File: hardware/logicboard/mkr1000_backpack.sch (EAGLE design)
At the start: 7 parts, among them J4 DNP, J5 DNP

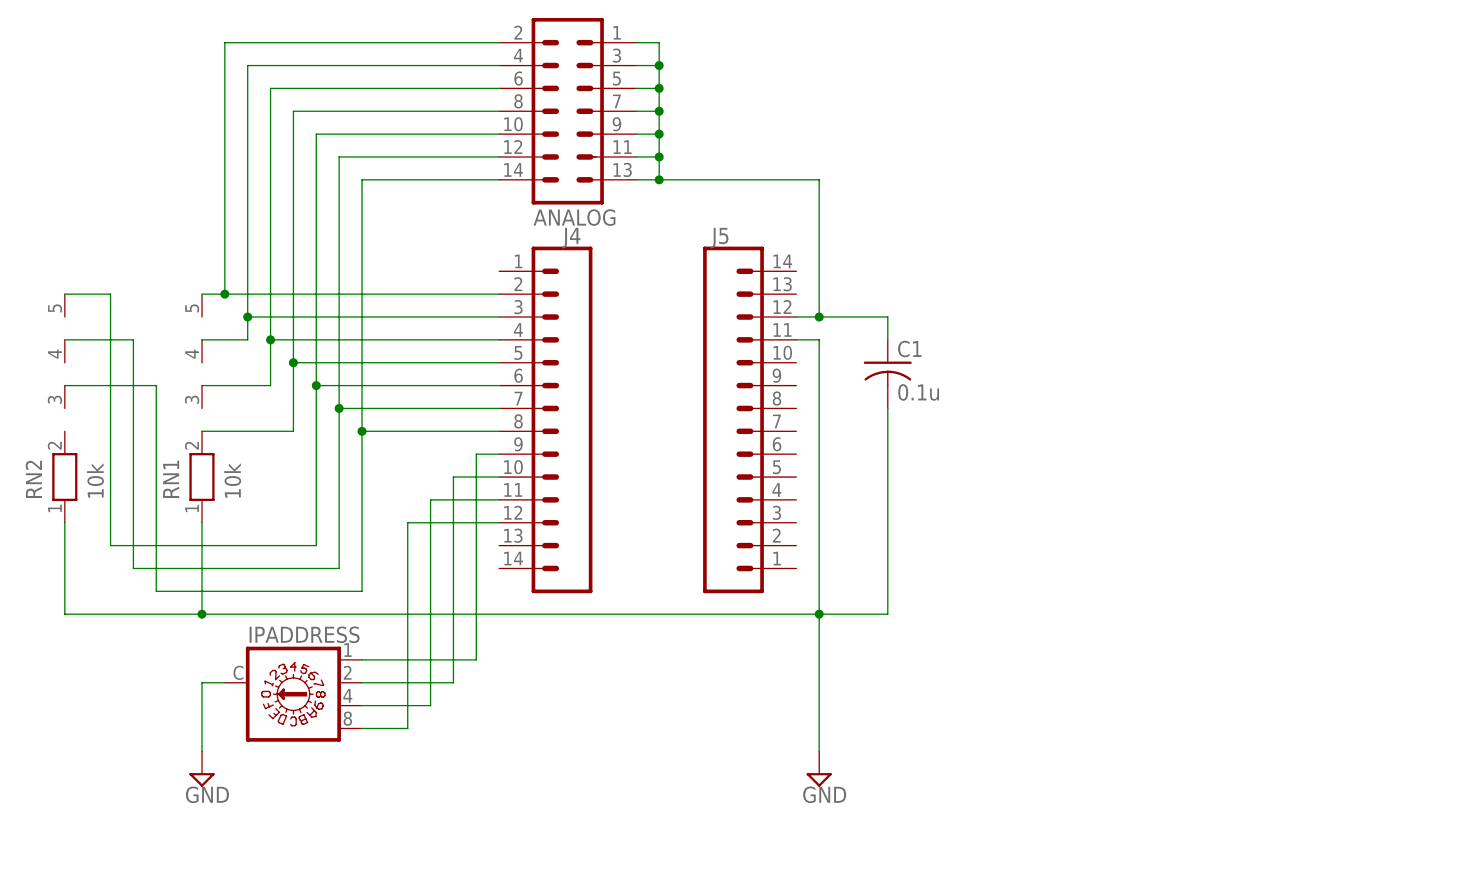
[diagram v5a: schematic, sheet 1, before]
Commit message: LED ports and I2C port.
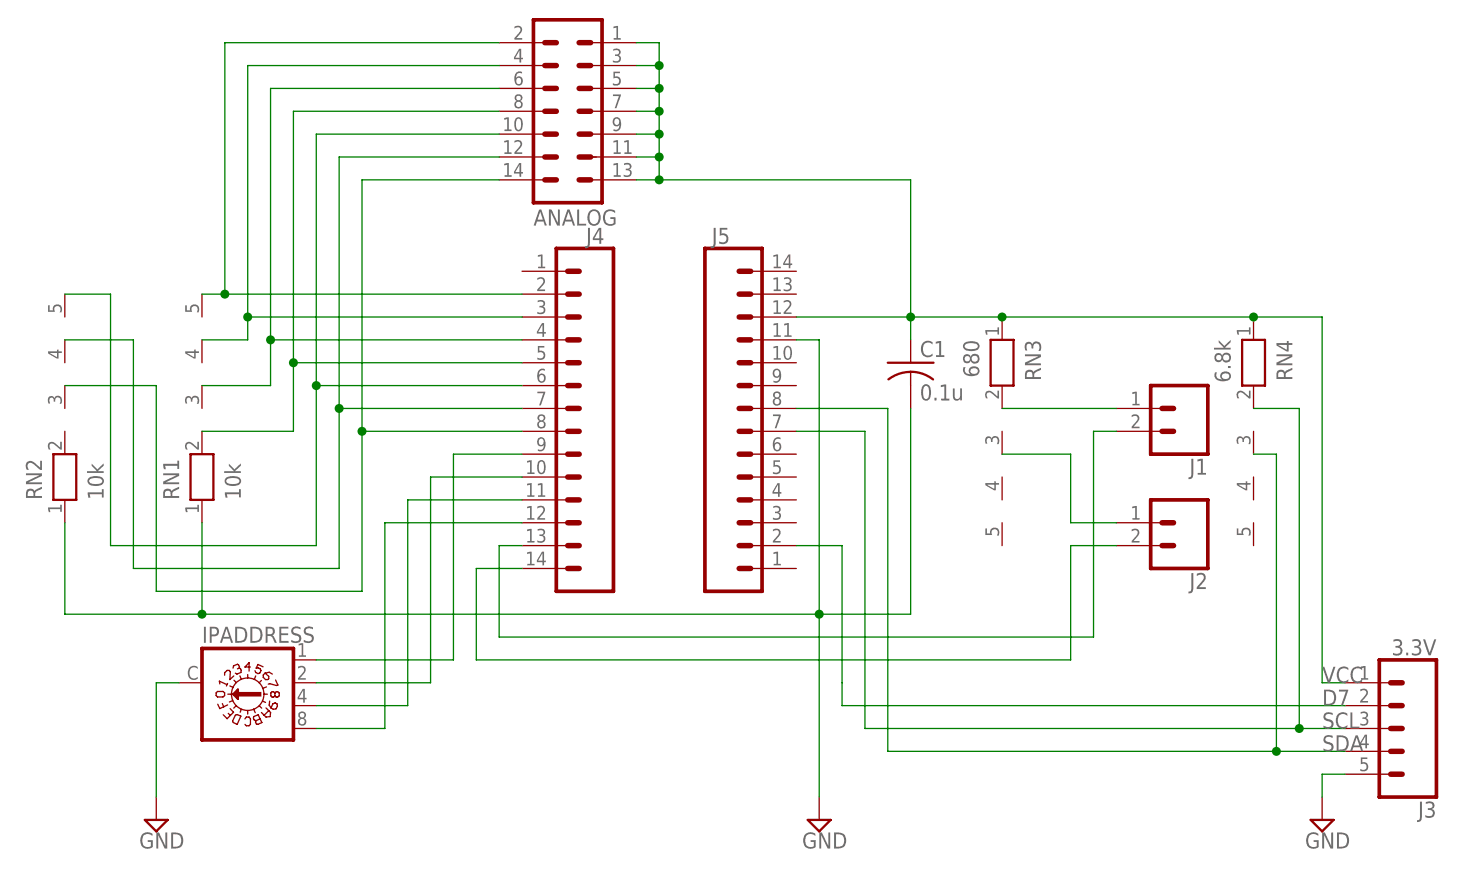
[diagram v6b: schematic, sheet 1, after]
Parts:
- added J1, J2: (no value), SparkFun-Connectors:CONN_02-JST-2-PTH-NO_SILK
- added J3: 3.3V, SparkFun-Connectors:CONN_05SMD
- added RN3: 680, resistor-net:RN04
- added RN4: 6.8k, resistor-net:RN04
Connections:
- new net D7: J3.2, J5.2
- new net N$1: J1.1, RN3.2
- new net N$2: J2.1, RN3.3
- new net N$3: J1.2, J4.13
- new net N$4: J2.2, J4.14
- new net SCL: J3.3, J5.7, RN4.2
- new net SDA: J3.4, J5.8, RN4.3
- net GND: now also J3.5
- net VCC: now also J3.1, RN3.1, RN4.1
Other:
- moved on the sheet: C1, IPADDRESS, J4

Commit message: SparkFun Triple Axis Accelerometer Breakout - H3LIS331DL Ready.
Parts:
- removed RN3: 680, resistor-net:RN04
- removed RN4: 6.8k, resistor-net:RN04
- added DUMMY, I2C: (no value), SparkFun-Connectors:CONN_04
- added R1, R2: 680, resistor:R-EU_0204/5
- added R3, R4: 6.8k, resistor:R-EU_0204/5
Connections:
- net GND: now also I2C.1
- net N$1: now also R1.1; no longer RN3.2
- net N$2: now also R2.1; no longer RN3.3
- net SCL: now also I2C.4, R4.1; no longer RN4.2
- net SDA: now also I2C.3, R3.1; no longer RN4.3
- net VCC: now also I2C.2, R1.2, R2.2, R3.2, R4.2; no longer RN3.1, RN4.1
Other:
- moved on the sheet: J1, J2, J3

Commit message: MMA8452Q
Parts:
- removed DUMMY, I2C: (no value), SparkFun-Connectors:CONN_04
- added MMA8452Q: (no value), SparkFun-Connectors:CONN_06NO_SILK_FEMALE_PTH
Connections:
- new net D6: J5.1, MMA8452Q.5
- net D7: now also MMA8452Q.4
- net GND: now also MMA8452Q.6; no longer I2C.1
- net SCL: now also MMA8452Q.3; no longer I2C.4
- net SDA: now also MMA8452Q.2; no longer I2C.3
- net VCC: now also MMA8452Q.1; no longer I2C.2
